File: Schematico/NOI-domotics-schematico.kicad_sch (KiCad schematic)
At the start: 6 parts

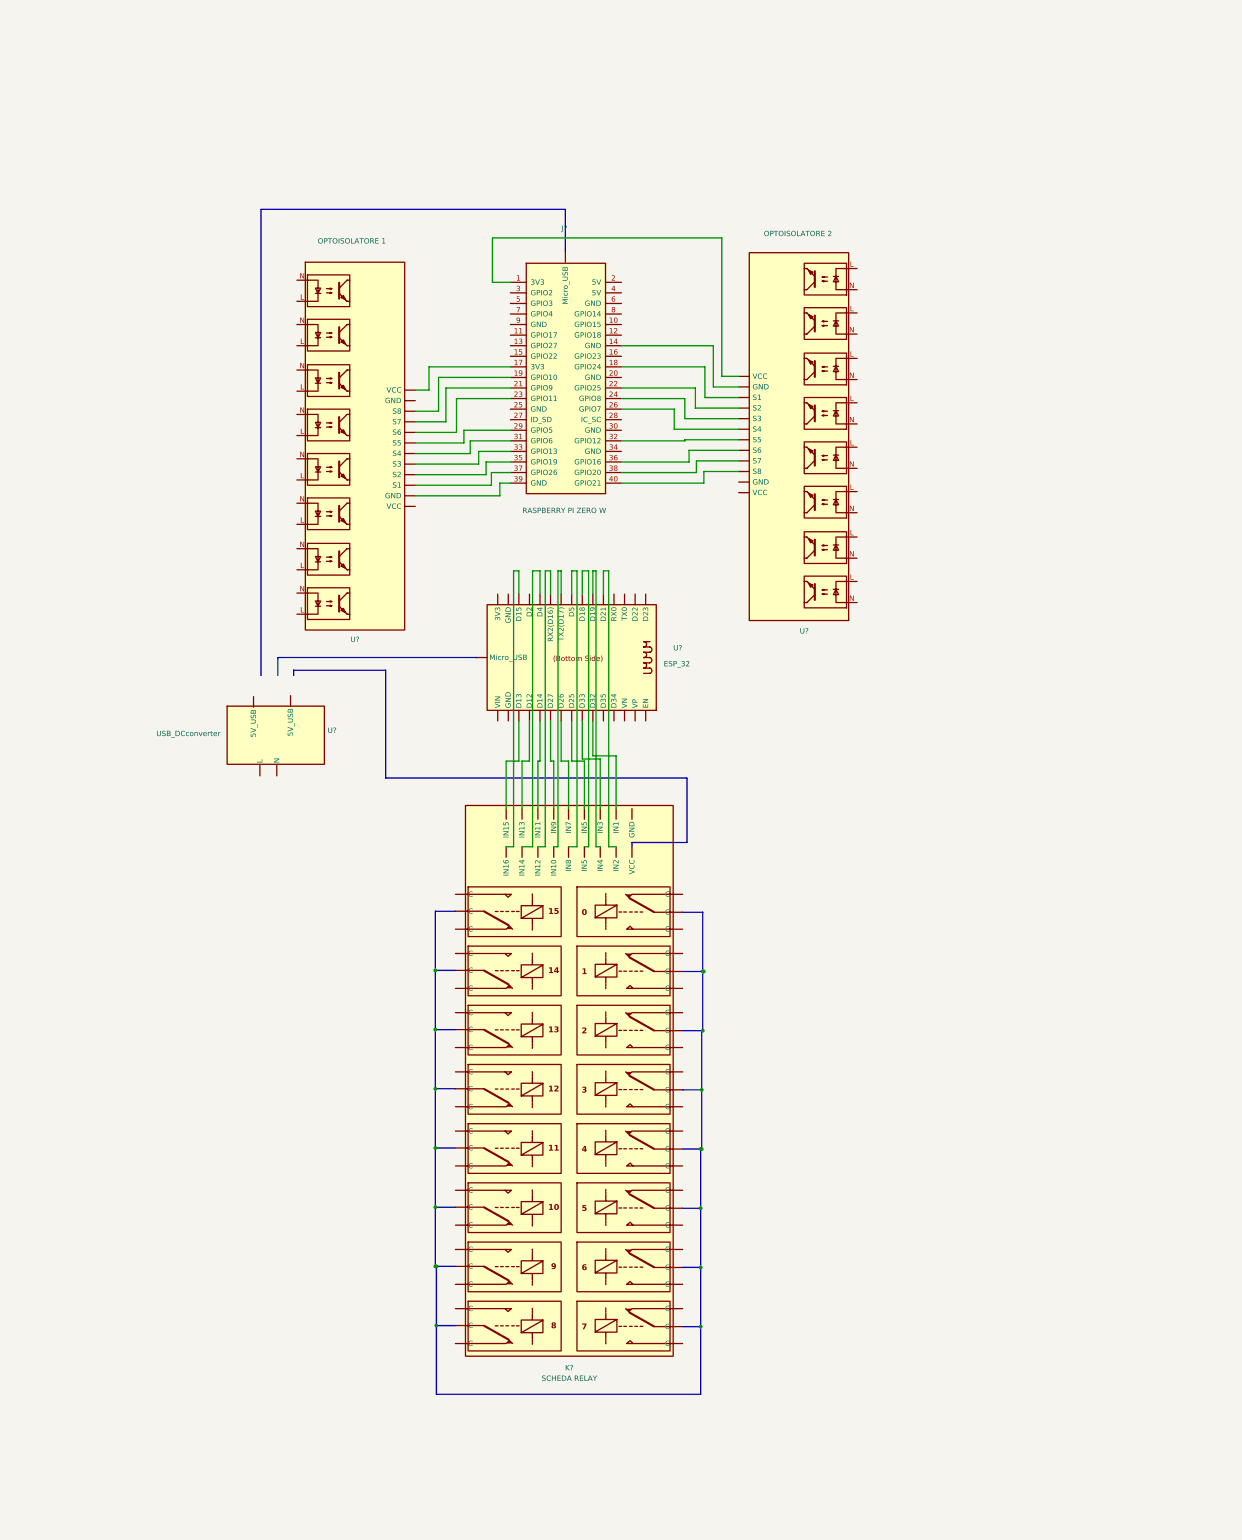
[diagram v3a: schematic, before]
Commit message: aggiunto relay base
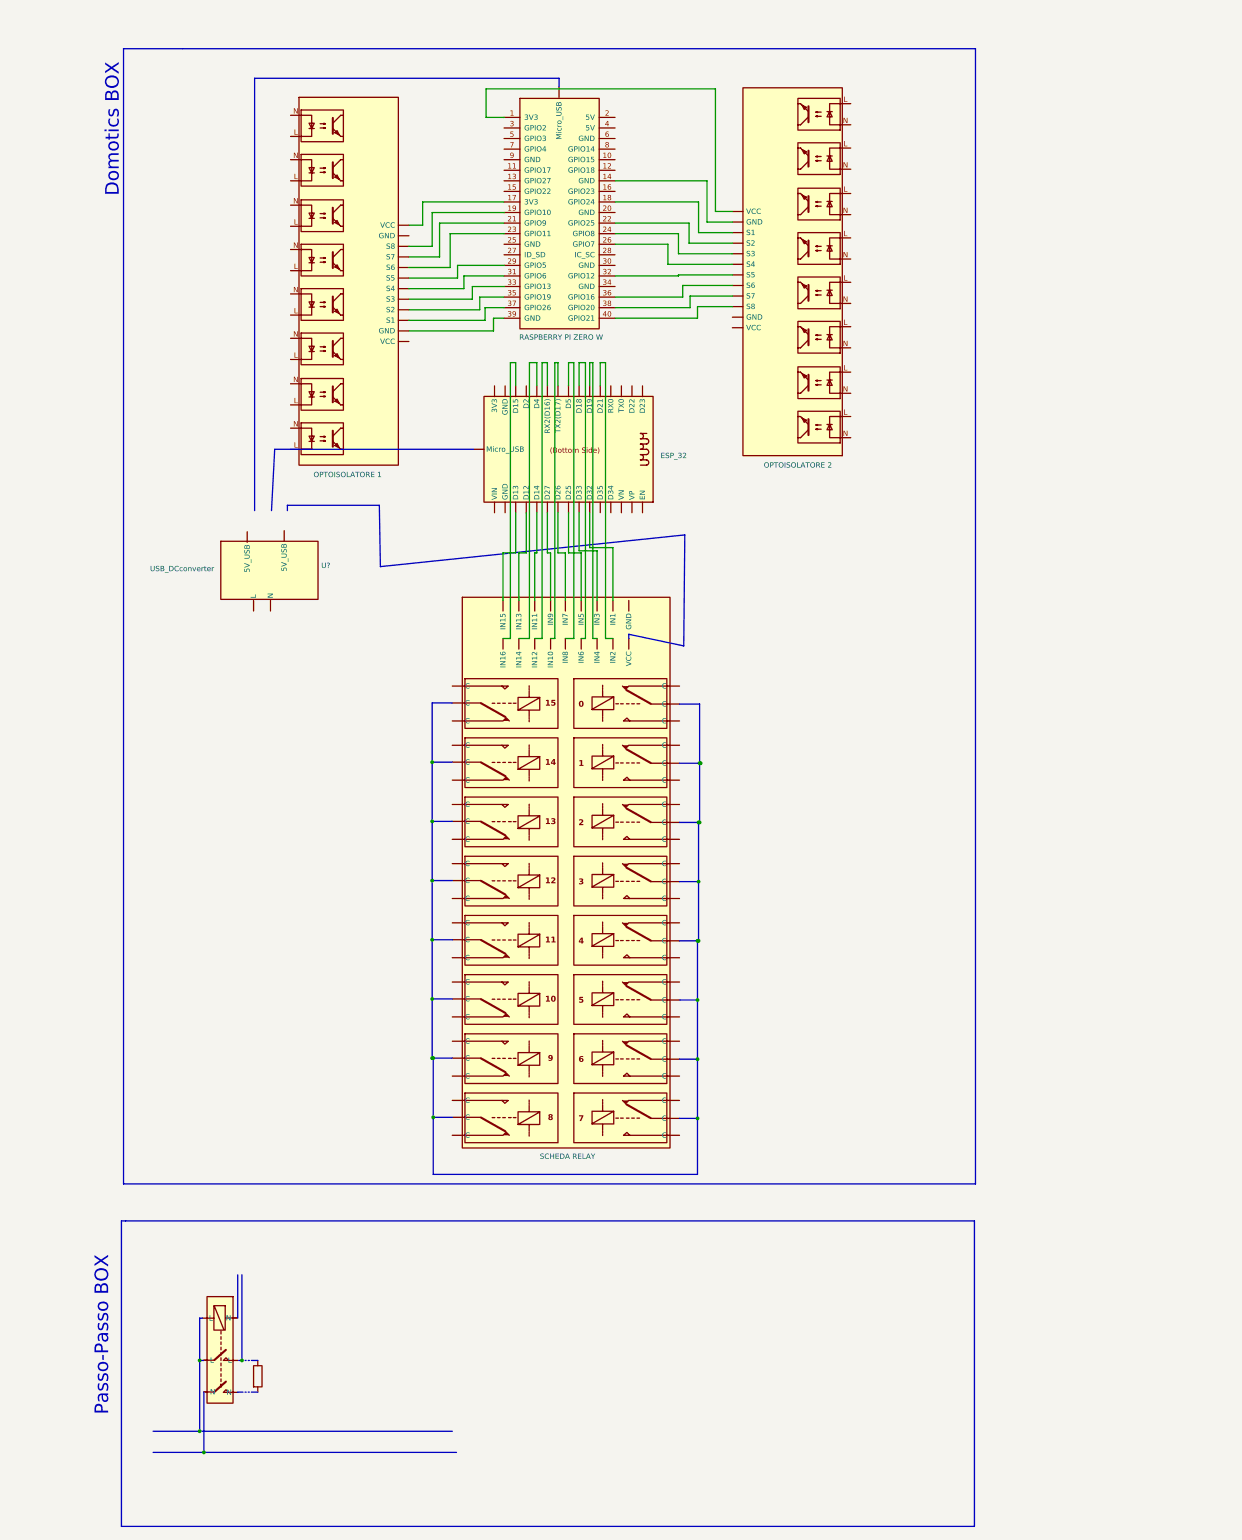
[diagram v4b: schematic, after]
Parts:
- added K?: (no value), Relay_THT:Relay_StandexMeder_DIP_LowProfile, symbol Relay:DIPxx-2Axx-21x
- added R?: (no value), symbol Device:R
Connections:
- net at U?. (VCC): now also J?.39 (GND)
- net at K?. (VCC): now also U?.1 (VP)
- net at U?.1 (VP): no longer K?. (VCC)
- new net: K?. (VCC), U?.1 (VP) (x15)
- now unconnected: U?.1 (VP), U?.1 (VP), U?.1 (VP), U?.1 (VP), U?.1 (VP), U?.1 (VP), U?.1 (VP), U?.1 (VP), U?.1 (VP), U?.1 (VP), U?.1 (VP), U?.1 (VP), U?.1 (VP), U?.1 (VP), U?.1 (VP)
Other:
- note added: "Domotics BOX"
- note added: "Passo-Passo BOX"
- moved on the sheet: U?

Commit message: jeje
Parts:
- removed K?: (no value), Relay_THT:Relay_StandexMeder_DIP_LowProfile, symbol Relay:DIPxx-2Axx-21x
- removed R?: (no value), symbol Device:R
- added K?: P13, Relay_THT:Relay_StandexMeder_DIP_LowProfile, symbol Relay:DIPxx-2Axx-21x
- added K?: P14, Relay_THT:Relay_StandexMeder_DIP_LowProfile, symbol Relay:DIPxx-2Axx-21x
- added K?: P15, Relay_THT:Relay_StandexMeder_DIP_LowProfile, symbol Relay:DIPxx-2Axx-21x
- added K?: P5, Relay_THT:Relay_StandexMeder_DIP_LowProfile, symbol Relay:DIPxx-2Axx-21x
- added K?: P3, Relay_THT:Relay_StandexMeder_DIP_LowProfile, symbol Relay:DIPxx-2Axx-21x
- added K?: P10, Relay_THT:Relay_StandexMeder_DIP_LowProfile, symbol Relay:DIPxx-2Axx-21x
- added K?: P8, Relay_THT:Relay_StandexMeder_DIP_LowProfile, symbol Relay:DIPxx-2Axx-21x
- added K?: P12, Relay_THT:Relay_StandexMeder_DIP_LowProfile, symbol Relay:DIPxx-2Axx-21x
- added K?: P6, Relay_THT:Relay_StandexMeder_DIP_LowProfile, symbol Relay:DIPxx-2Axx-21x
- added K?: P11, Relay_THT:Relay_StandexMeder_DIP_LowProfile, symbol Relay:DIPxx-2Axx-21x
- added K?: P1, Relay_THT:Relay_StandexMeder_DIP_LowProfile, symbol Relay:DIPxx-2Axx-21x
- added K?: P2, Relay_THT:Relay_StandexMeder_DIP_LowProfile, symbol Relay:DIPxx-2Axx-21x
- added K?: P4, Relay_THT:Relay_StandexMeder_DIP_LowProfile, symbol Relay:DIPxx-2Axx-21x
- added K?: P9, Relay_THT:Relay_StandexMeder_DIP_LowProfile, symbol Relay:DIPxx-2Axx-21x
- added K?: P16, Relay_THT:Relay_StandexMeder_DIP_LowProfile, symbol Relay:DIPxx-2Axx-21x
- added K?: P7, Relay_THT:Relay_StandexMeder_DIP_LowProfile, symbol Relay:DIPxx-2Axx-21x
- added R? (x16): LOAD, symbol Device:R
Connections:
- net at U?. (VCC): now also J?.39 (GND)
- net at K?. (VCC): now also U?.1 (VP)
- net at U?.1 (VP): no longer K?. (VCC)
- new net: K?. (VCC), U?.1 (VP) (x15)
- now unconnected: U?.1 (VP), U?.1 (VP), U?.1 (VP), U?.1 (VP), U?.1 (VP), U?.1 (VP), U?.1 (VP), U?.1 (VP), U?.1 (VP), U?.1 (VP), U?.1 (VP), U?.1 (VP), U?.1 (VP), U?.1 (VP), U?.1 (VP)
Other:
- moved on the sheet: U?

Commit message: cococo
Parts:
- removed R?: LOAD, symbol Device:R
- added R?: LOAD, symbol Device:R
- added RN?: R_Network07_US, Resistor_THT:R_Array_SIP8, symbol Device:R_Network07_US
- added U?: (no value), symbol USB_5V:USB_DCconverter
- K?: value P13 -> (none)
- K?: value P14 -> (none)
- K?: value P15 -> (none)
- K?: value P5 -> (none)
- K?: value P3 -> (none)
- K?: value P10 -> (none)
- K?: value P8 -> (none)
- K?: value P12 -> (none)
- K?: value P6 -> (none)
- K?: value P11 -> (none)
- K?: value P1 -> (none)
- K?: value P2 -> (none)
- K?: value P4 -> (none)
- K?: value P9 -> (none)
- K?: value P16 -> (none)
- K?: value P7 -> (none)
- U?: value USB_DCconverter -> Alimentatore Doppio USB
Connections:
- net at U?. (VCC): now also J?.39 (GND)
- net at J?. (Micro_USB): now also U?. (N)
- net at U?. (N): now also U?. (Micro_USB)
- net at K?. (VCC): now also U?.1 (VP)
- net at U?.1 (VP): no longer K?. (VCC)
- new net: K?. (VCC), RN?.
- new net: RN?., U?.1 (VP)
- new net: K?. (VCC), U?.1 (VP) (x15)
- now unconnected: U?.1 (VP), U?.1 (VP), U?.1 (VP), U?.1 (VP), U?.1 (VP), U?.1 (VP), U?.1 (VP), U?.1 (VP), U?.1 (VP), U?.1 (VP), U?.1 (VP), U?.1 (VP), U?.1 (VP), U?.1 (VP), U?.1 (VP)

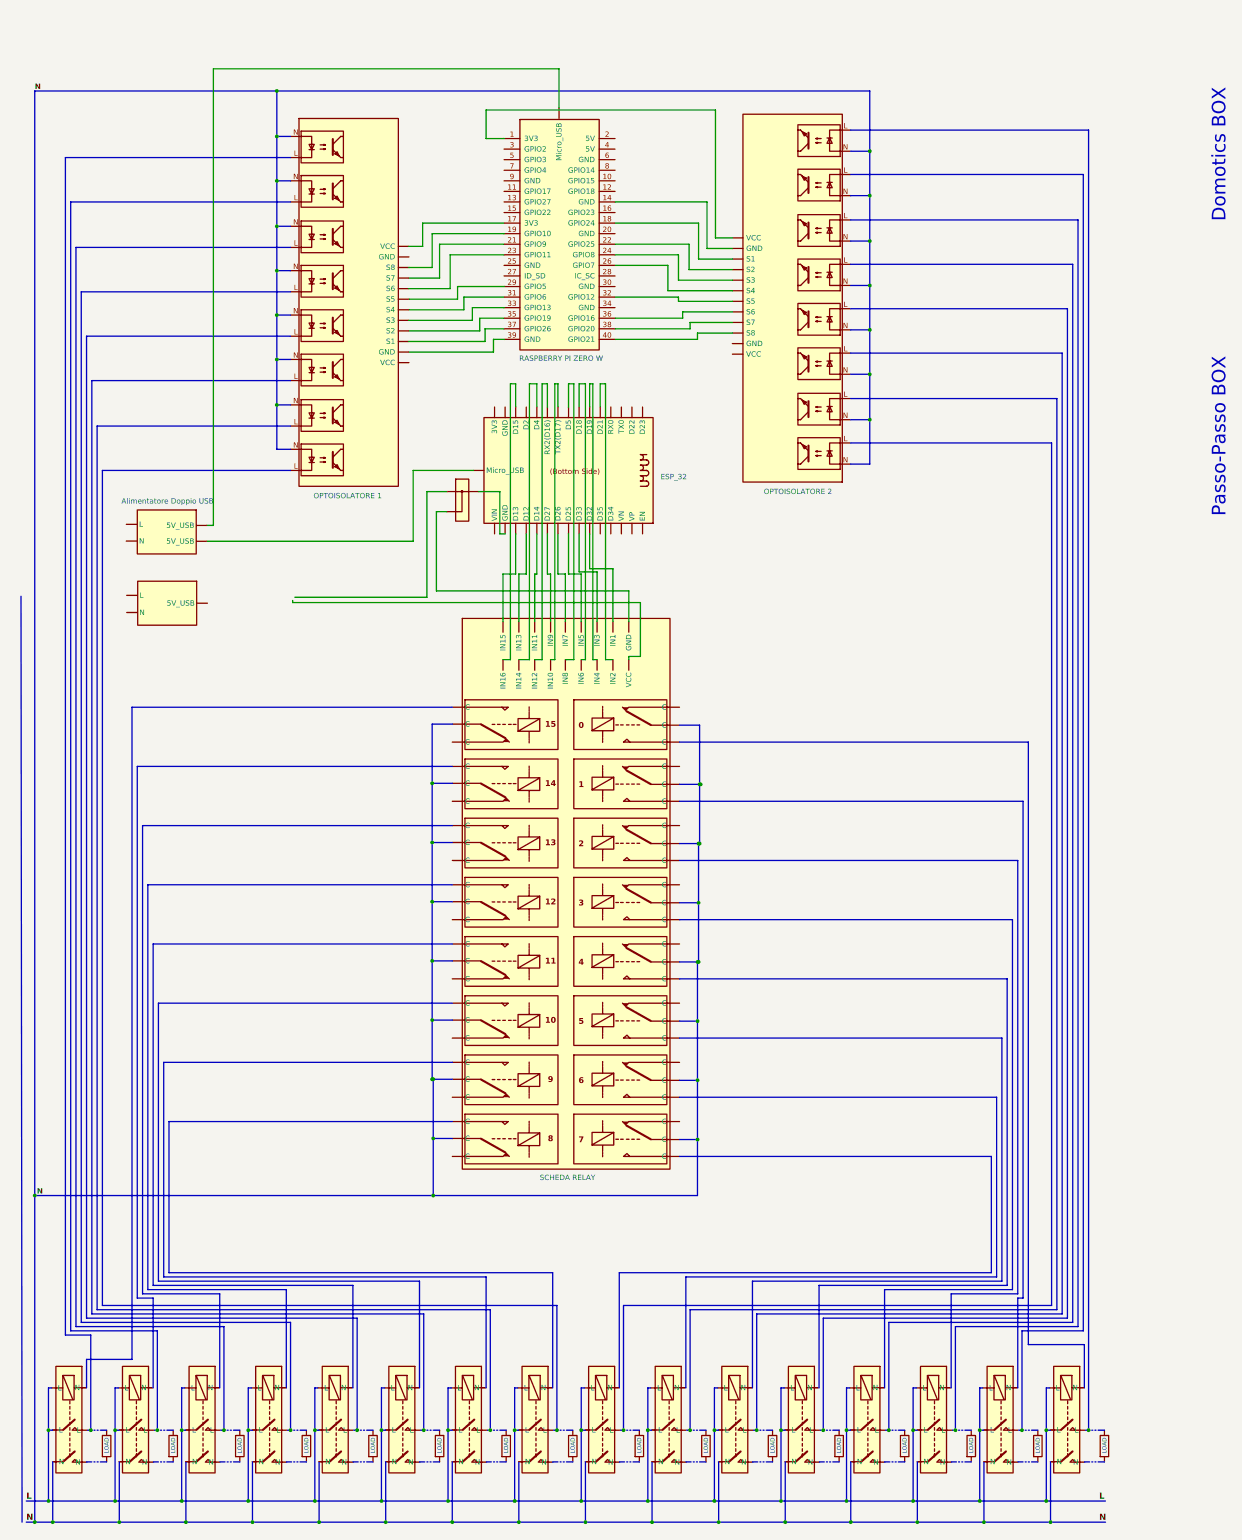
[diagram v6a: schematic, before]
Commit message: schematic completed
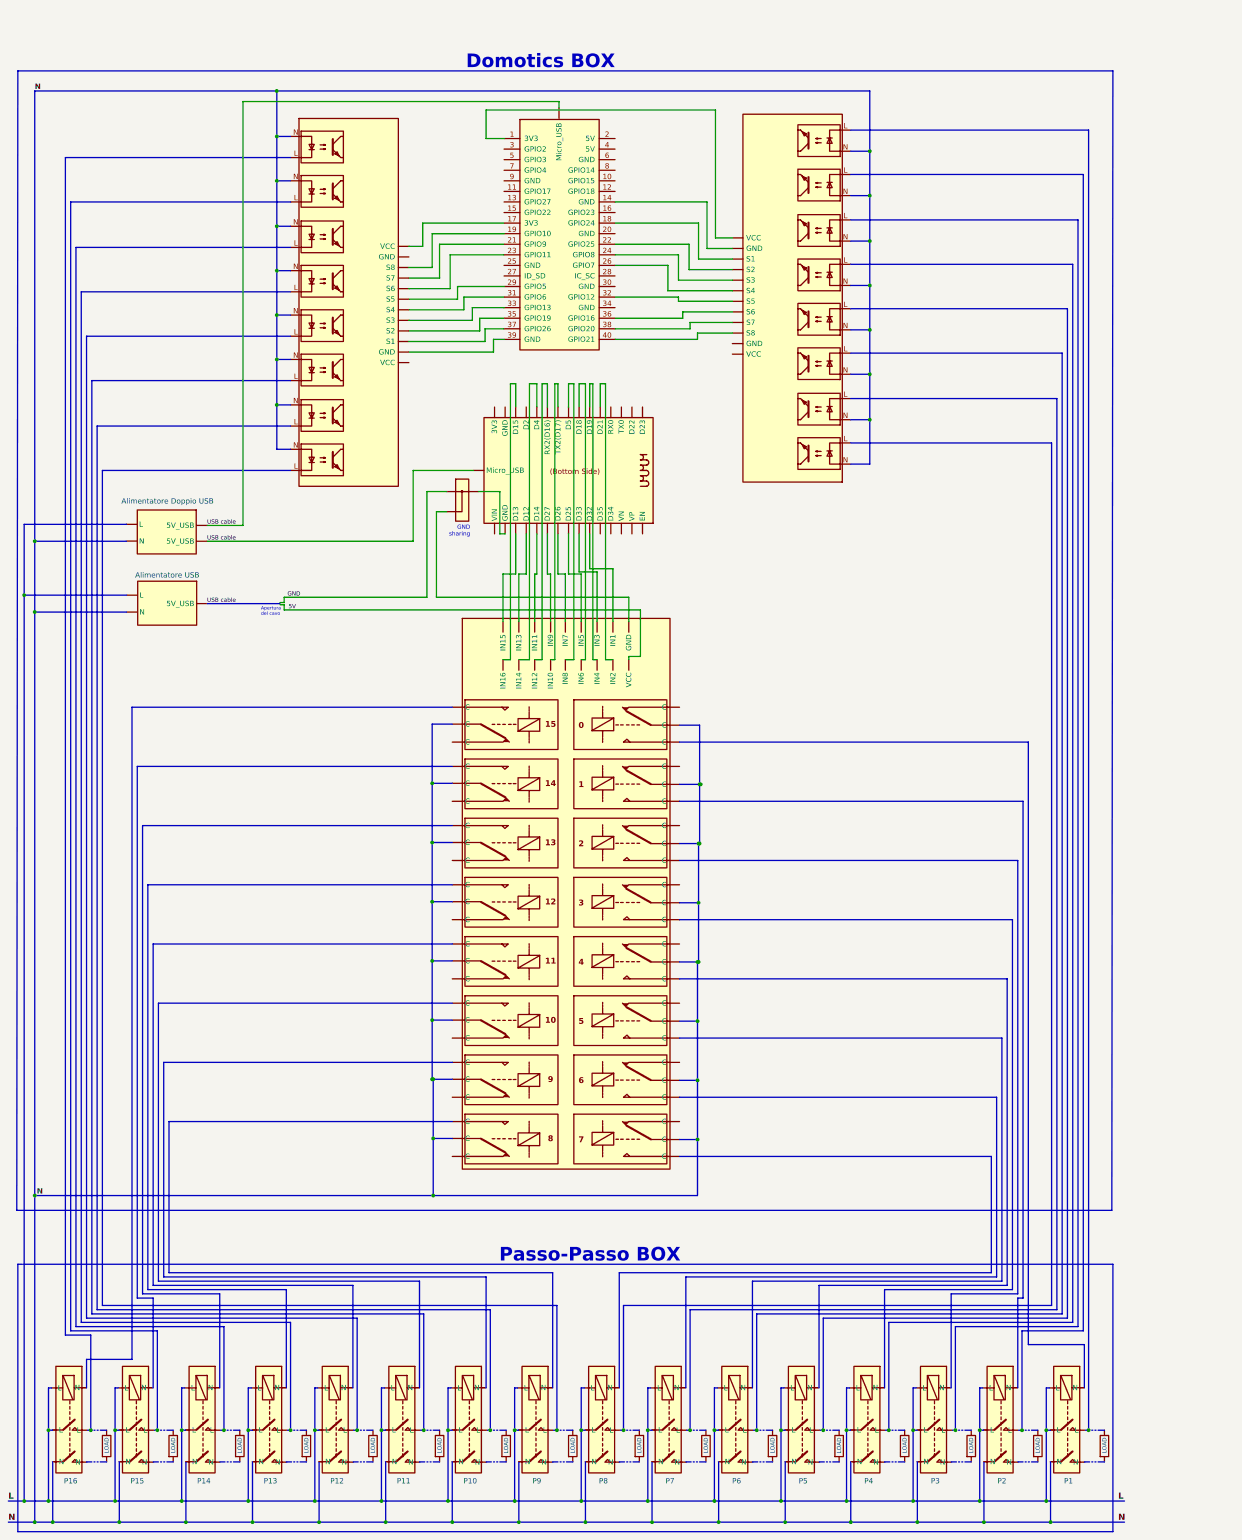
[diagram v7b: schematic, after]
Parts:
- J?: value RASPBERRY PI ZERO W -> (none)
- K?: value (none) -> P4
- K?: value (none) -> P3
- K?: value (none) -> P2
- K?: value (none) -> P12
- K?: value (none) -> P14
- K?: value (none) -> P7
- K?: value (none) -> P9
- K?: value (none) -> P5
- K?: value (none) -> P11
- K?: value (none) -> P6
- K?: value (none) -> P16
- K?: value (none) -> P15
- K?: value SCHEDA RELAY -> (none)
- K?: value (none) -> P13
- K?: value (none) -> P8
- K?: value (none) -> P1
- K?: value (none) -> P10
- U?: value OPTOISOLATORE 1 -> (none)
- U?: value (none) -> Alimentatore USB
- U?: value ESP_32 -> (none)
- U?: value OPTOISOLATORE 2 -> (none)
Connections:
- net at U?. (VCC): now also J?.39 (GND)
- net USB cable: now reaches J?. (Micro_USB), U?. (N)
- net USB cable: now also U?. (Micro_USB), U?. (N)
- net GND: now reaches RN?.
- net 5V: now reaches K?. (VCC)
- net 5V: no longer RN?.
- net at U?.1 (VP): no longer RN?.
- new net: K?. (VCC), RN?.
- new net: RN?., U?.1 (VP)
- new net: K?. (VCC), U?.1 (VP) (x16)
- now unconnected: U?.1 (VP), U?.1 (VP), U?.1 (VP), U?.1 (VP), U?.1 (VP), U?.1 (VP), U?.1 (VP), U?.1 (VP), U?.1 (VP), U?.1 (VP), U?.1 (VP), U?.1 (VP), U?.1 (VP), U?.1 (VP), U?.1 (VP), U?.1 (VP)
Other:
- note added: "Apertura del cavo"
- note added: "GND sharing"

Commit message: Schematico completato
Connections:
- net at U?. (VCC): now also J?.39 (GND)
- net at U?.1 (VP): no longer RN?.
- new net: K?. (VCC), RN?.
- new net: RN?., U?.1 (VP)
- new net: K?. (VCC), U?.1 (VP) (x16)
- now unconnected: U?.1 (VP), U?.1 (VP), U?.1 (VP), U?.1 (VP), U?.1 (VP), U?.1 (VP), U?.1 (VP), U?.1 (VP), U?.1 (VP), U?.1 (VP), U?.1 (VP), U?.1 (VP), U?.1 (VP), U?.1 (VP), U?.1 (VP), U?.1 (VP)
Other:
- title: (none) -> NOI Domotics
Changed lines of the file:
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@@
   (paper "A3" portrait)
   (title_block
-    (date "2025-03-03")
+    (title "NOI Domotics")
+    (date "2025-03-04")
+    (comment 1 "Designed by Marco Benetti & Filippo Zeggio")
   )
   (junction (at 71.12 367.284) (diameter 0) (color 0 0 0 0)
